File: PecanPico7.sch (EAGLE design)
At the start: 177 parts, among them IC1 Si4464-B1B-FM, IC10 TC1185-1.8VCT713, IC11 TC1185-2.5VCT713, IC12 ADR380ARTZ, IC13 RF6886, IC15 MPU-9250, IC16 PAC1720-1-AIA-TR, IC2 Si4464-B1B-FM, IC3 BME280_BME280, IC4 UBLOX_MAX-6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

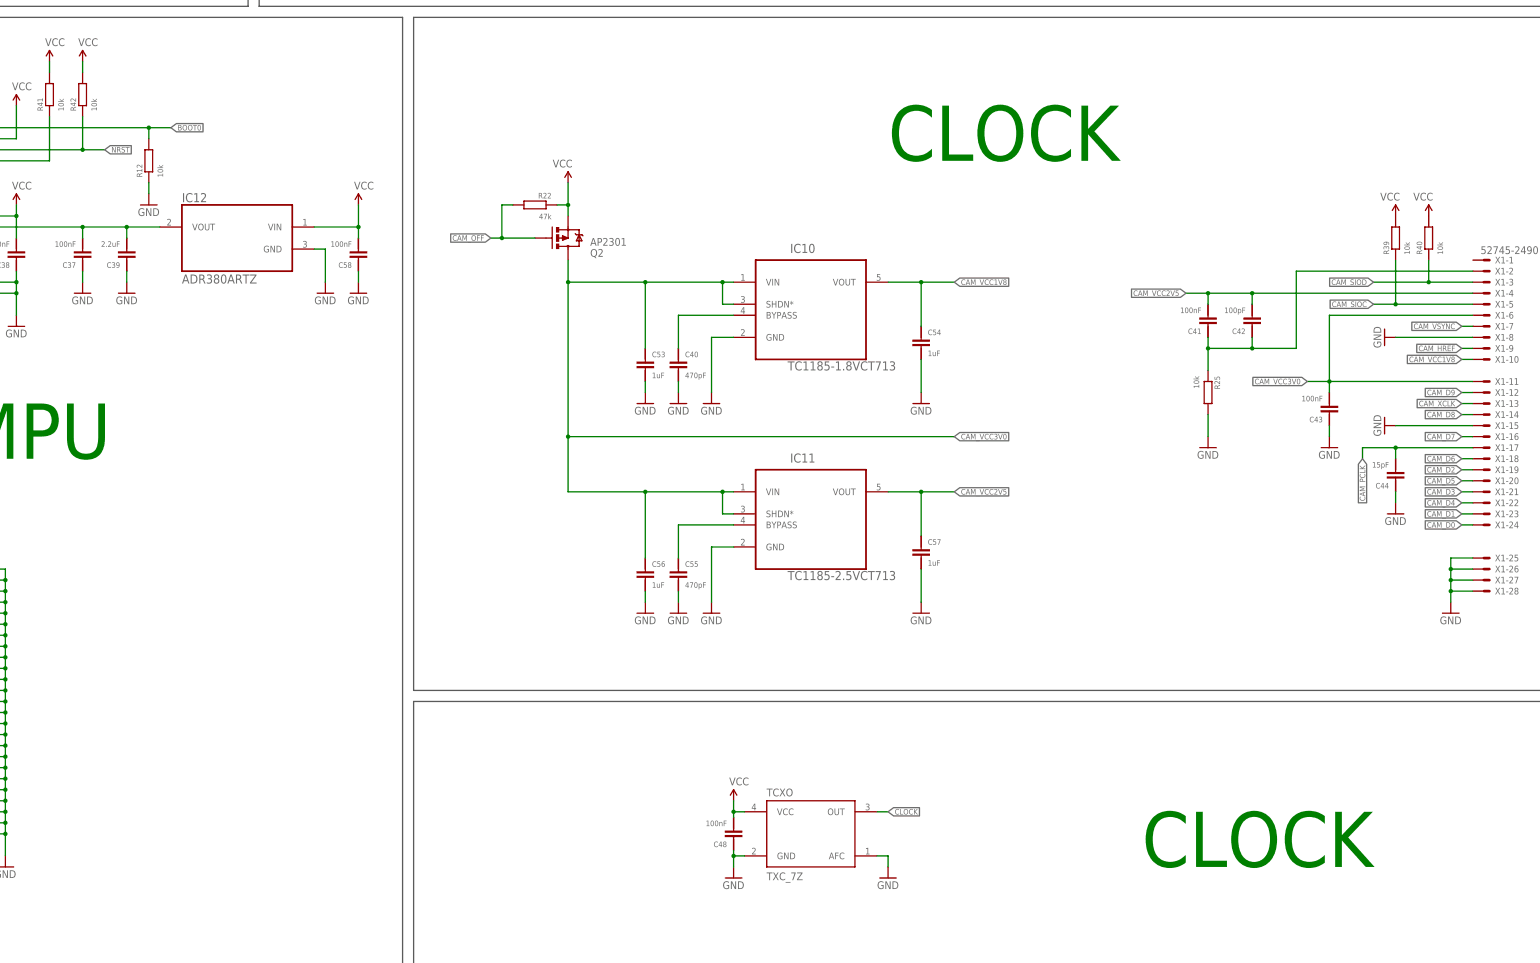
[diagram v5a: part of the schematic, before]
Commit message: Fixed incorrect voltage supply at OV2640
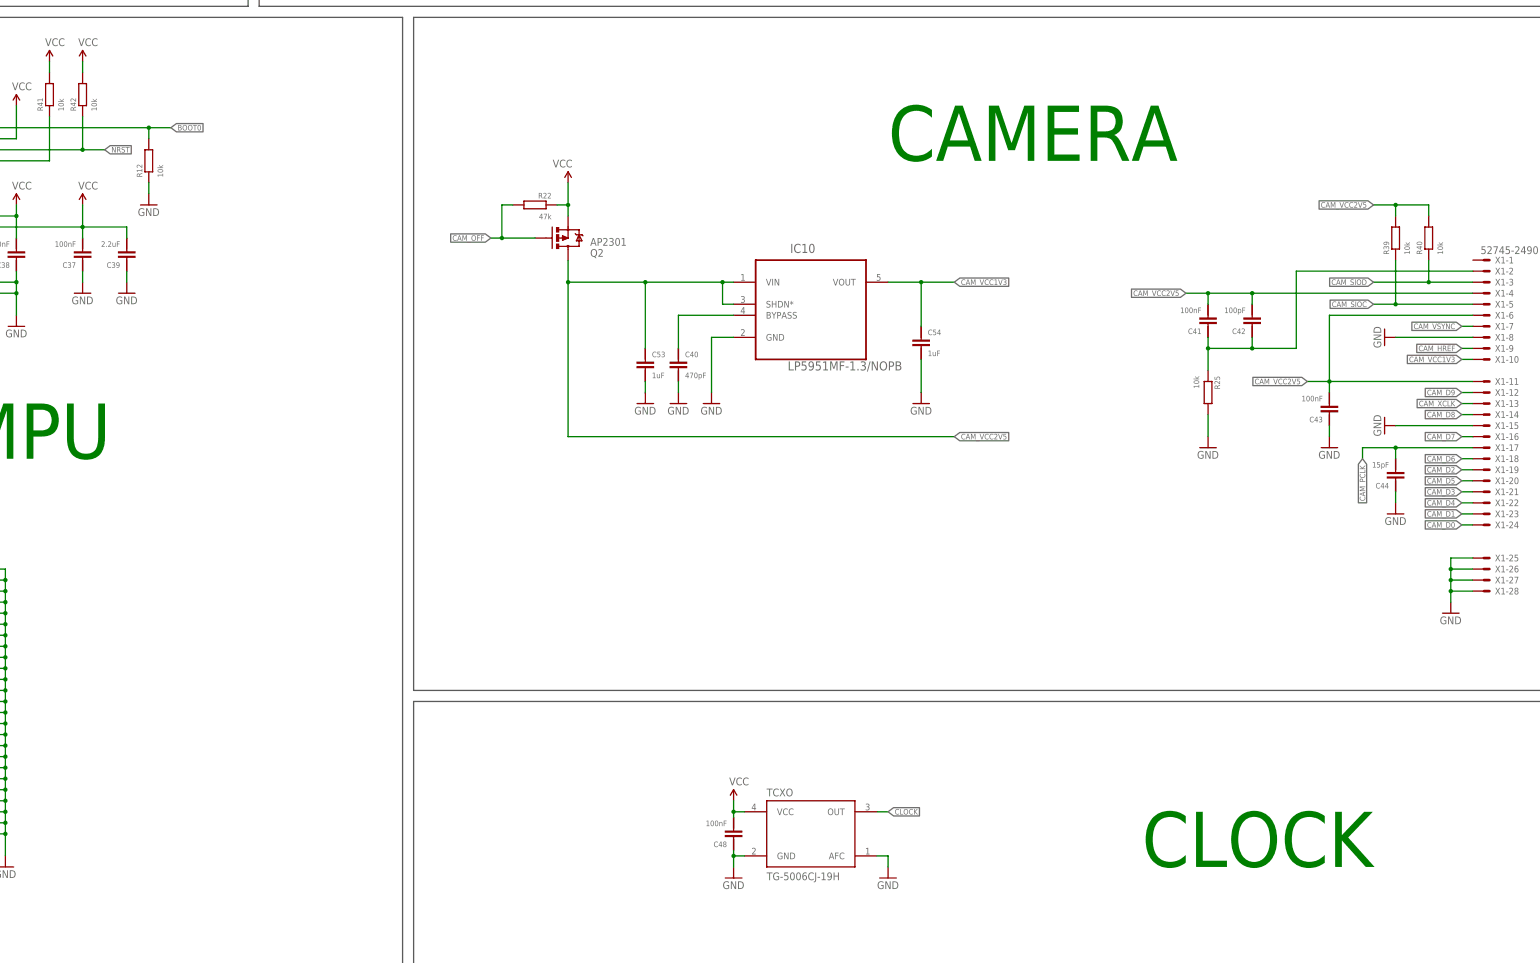
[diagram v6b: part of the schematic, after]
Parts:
- removed C55: 470pF, PecanPico6:CAP-0402
- removed C56, C57: 1uF, PecanPico6:CAP-0402
- removed C58: 100nF, PecanPico6:CAP-0402
- removed IC11: TC1185-2.5VCT713, stm32f42x:TC1185-1.8VCT713
- removed IC12: ADR380ARTZ, stm32f4:ADR380ARTZ
- IC10: value TC1185-1.8VCT713 -> LP5951MF-1.3/NOPB
- TCXO: value TXC_7Z -> TG-5006CJ-19H
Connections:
- net CAM_VCC1V8 renamed CAM_VCC1V3
- removed net CAM_VCC3V0: C43.1, C53.2, C56.2, IC10.SHDN*, IC10.VIN, IC11.SHDN*, IC11.VIN, Q2.D, X1-11.S, X1-6.S
- removed net N$28: C55.2, IC11.BYPASS
- removed net N$30: C37.1, C39.1, IC12.VOUT, IC5G$3.VREF+
- net CAM_VCC2V5: now also C43.1, C53.2, IC10.SHDN*, IC10.VIN, Q2.D, R39.2, R40.2, X1-11.S, X1-6.S; no longer C57.2, IC11.VOUT
- net GND: no longer C55.1, C56.1, C57.1, C58.2, IC11.GND, IC12.GND
- net VCC: now also C37.1, C39.1, IC5G$3.VREF+; no longer C58.1, IC12.VIN, R39.2, R40.2
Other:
- note added: "CAMERA"

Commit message: Relocated names, added infos, added PCB name
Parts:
- added LOGO1: OSHW-LOGOL, PecanPico6:OSHW-LOGOL
- IC10: value LP5951MF-1.3/NOPB -> TC1185-1.8VCT713
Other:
- note added: "Camera OV2640 OV9655"
- note added: "Camera connector for OV9655 or OV2640"
- note added: "DVVD needed 1.30V 1.80V"
- note added: "IC10 LP5951MF-1.3/NOPB TC1185-1.8VCT713"
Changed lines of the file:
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@@
 <?xml version="1.0" encoding="utf-8"?>
 <!DOCTYPE eagle SYSTEM "eagle.dtd">
-<eagle version="7.2.0">
+<eagle version="7.3.0">
 <drawing>
 <settings>
@@
 <part name="C52" library="PecanFemto3" deviceset="CAP-0805" device="" value="10uF"/>
 <part name="GND72" library="PecanPico6" deviceset="GND" device=""/>
-<part name="IC10" library="stm32f42x" deviceset="TC1185-1.8VCT713" device="" value="LP5951MF-1.3/NOPB"/>
+<part name="IC10" library="stm32f42x" deviceset="TC1185-1.8VCT713" device="" value=""/>
 <part name="C40" library="PecanPico6" deviceset="CAP-0402" device="" value="470pF"/>
 <part name="C53" library="PecanPico6" deviceset="CAP-0402" device="" value="1uF"/>
@@
 <part name="X1" library="con-molex" deviceset="52745-2490" device=""/>
 <part name="P+26" library="PecanPico6" deviceset="3.3V" device="" value="VCC"/>
+<part name="LOGO1" library="PecanPico6" deviceset="OSHW-LOGO" device="L"/>
 </parts>
 <sheets>
@@
 <wire x1="83.82" y1="27.94" x2="83.82" y2="91.44" width="0.1524" layer="97"/>
 <text x="251.46" y="53.34" size="12.7" layer="91">CLOCK</text>
-<text x="193.04" y="215.9" size="12.7" layer="91">CAMERA</text>
+<text x="149.86" y="218.44" size="12.7" layer="91">CAMERA</text>
 <text x="215.9" y="340.36" size="12.7" layer="91">RADIOS</text>
 <text x="-233.68" y="452.12" size="12.7" layer="91">POWER
@@
 - All components are switchable for power saving</text>
 <text x="-256.54" y="558.8" size="5.08" layer="91">Features</text>
+<text x="170.18" y="132.08" size="1.778" layer="97">Camera
+OV2640
+OV9655</text>
+<text x="182.88" y="132.08" size="1.778" layer="97">DVVD needed
+1.30V
+1.80V</text>
+<text x="200.66" y="132.08" size="1.778" layer="97">IC10
+LP5951MF-1.3/NOPB
+TC1185-1.8VCT713</text>
+<wire x1="167.64" y1="142.24" x2="175.26" y2="142.24" width="0.1524" layer="97"/>
+<wire x1="175.26" y1="142.24" x2="228.6" y2="142.24" width="0.1524" layer="97"/>
+<wire x1="228.6" y1="142.24" x2="228.6" y2="129.54" width="0.1524" layer="97"/>
+<wire x1="228.6" y1="129.54" x2="167.64" y2="129.54" width="0.1524" layer="97"/>
+<wire x1="167.64" y1="129.54" x2="167.64" y2="142.24" width="0.1524" layer="97"/>
+<wire x1="175.26" y1="167.64" x2="175.26" y2="142.24" width="0.1524" layer="97"/>
+<wire x1="157.48" y1="142.24" x2="149.86" y2="129.54" width="0.1524" layer="97"/>
+<wire x1="149.86" y1="129.54" x2="165.1" y2="129.54" width="0.1524" layer="97"/>
+<wire x1="165.1" y1="129.54" x2="157.48" y2="142.24" width="0.1524" layer="97"/>
+<wire x1="157.48" y1="139.7" x2="157.48" y2="134.62" width="0.1524" layer="97"/>
+<circle x="157.48" y="132.08" radius="0.635" width="0" layer="97"/>
+<text x="312.42" y="218.44" size="2.54" layer="97">Camera connector for
+OV9655 or OV2640</text>
 </plain>
 <instances>
@@
 <instance part="X1" gate="-28" x="330.2" y="116.84"/>
 <instance part="P+26" gate="G$1" x="7.62" y="205.74"/>
+<instance part="LOGO1" gate="G$1" x="30.48" y="546.1"/>
 </instances>
 <busses>

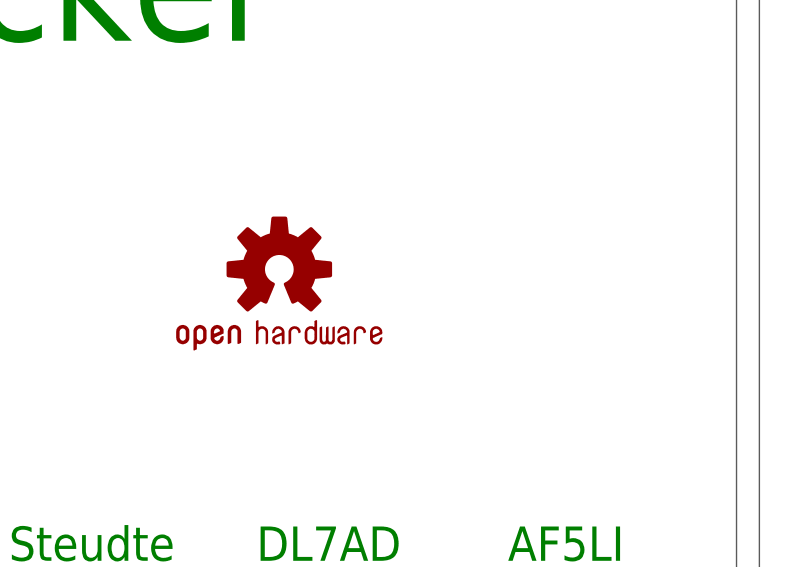
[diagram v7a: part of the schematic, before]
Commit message: Adjusted symbols
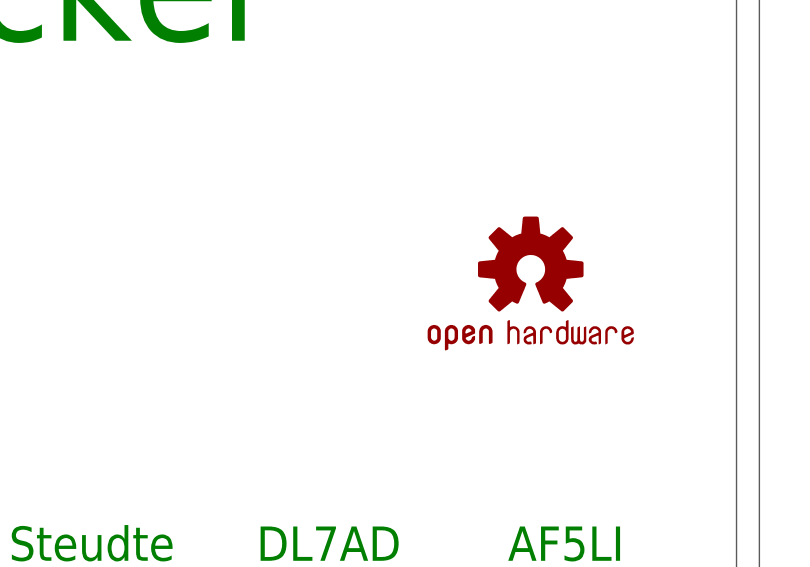
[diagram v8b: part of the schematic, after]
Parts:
- removed LOGO1: OSHW-LOGOL, PecanPico6:OSHW-LOGOL
- added LOGO2: OSHW-LOGOM, PecanPico6:OSHW-LOGOM
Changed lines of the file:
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@@
 <part name="X1" library="con-molex" deviceset="52745-2490" device=""/>
 <part name="P+26" library="PecanPico6" deviceset="3.3V" device="" value="VCC"/>
-<part name="LOGO1" library="PecanPico6" deviceset="OSHW-LOGO" device="L"/>
+<part name="LOGO2" library="PecanPico6" deviceset="OSHW-LOGO" device="M"/>
 </parts>
 <sheets>
@@
 <instance part="X1" gate="-28" x="330.2" y="116.84"/>
 <instance part="P+26" gate="G$1" x="7.62" y="205.74"/>
-<instance part="LOGO1" gate="G$1" x="30.48" y="546.1"/>
+<instance part="LOGO2" gate="G$1" x="58.42" y="546.1"/>
 </instances>
 <busses>
